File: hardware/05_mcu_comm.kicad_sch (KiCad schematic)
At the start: 0 parts

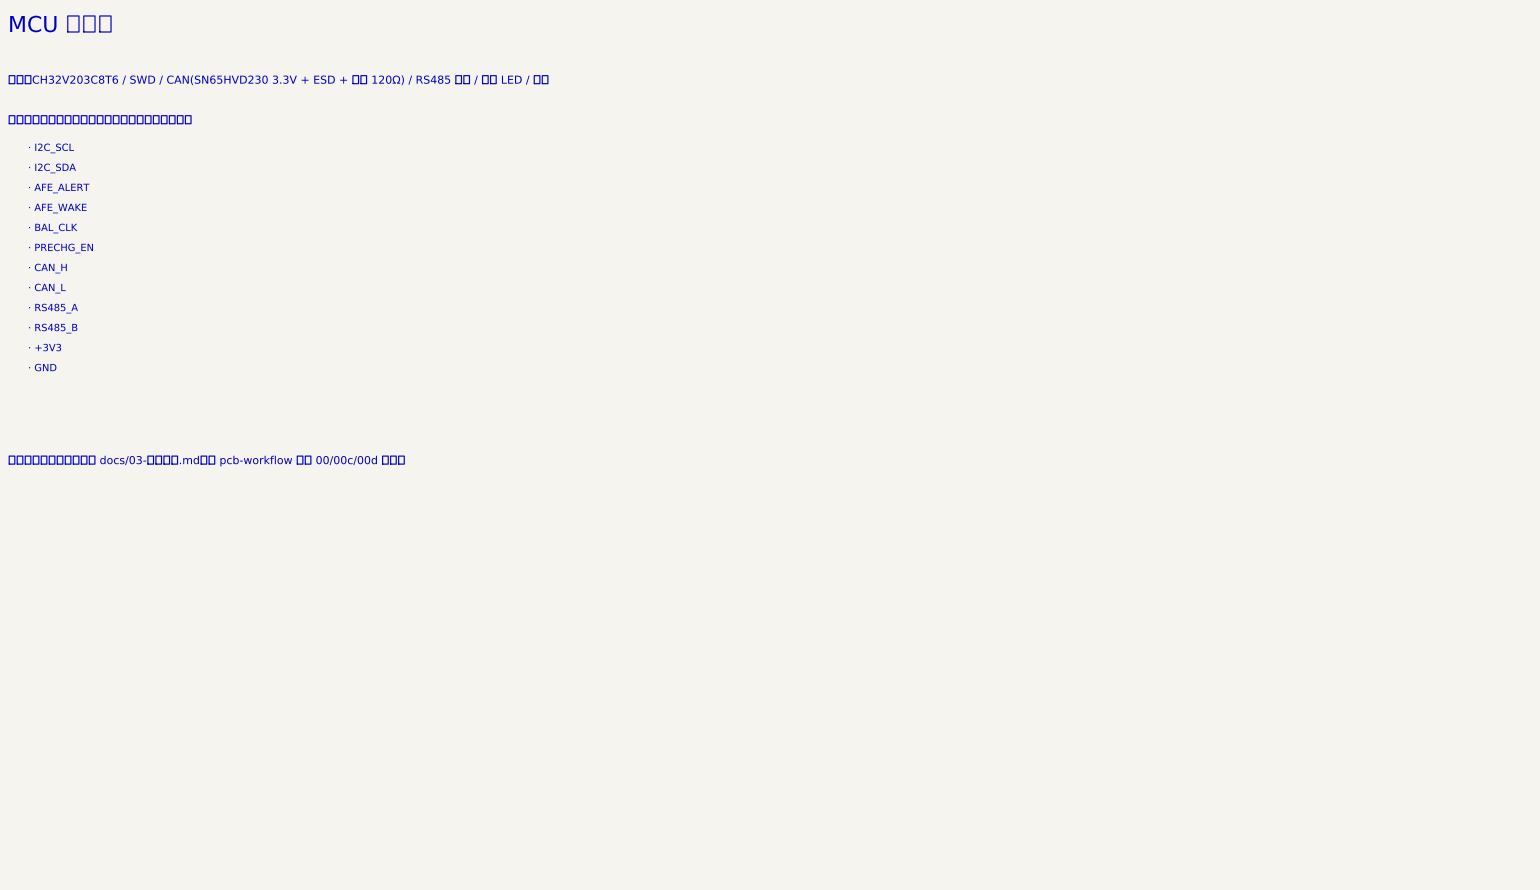
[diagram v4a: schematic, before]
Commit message: 05 页第 1 轮（DeepSeek，结尾因 API 余额不足 402 中断）：32 器件，ERC 仅跨页 isolated_pin_label，几何自检通过；取库 JP1 C492401
Co-Authored-By: Claude Opus 5.5 <noreply@anthropic.com>
Claude-Session: https://claude.ai/code/session_018LcBBXJnjJ1MVmds7Fkezv
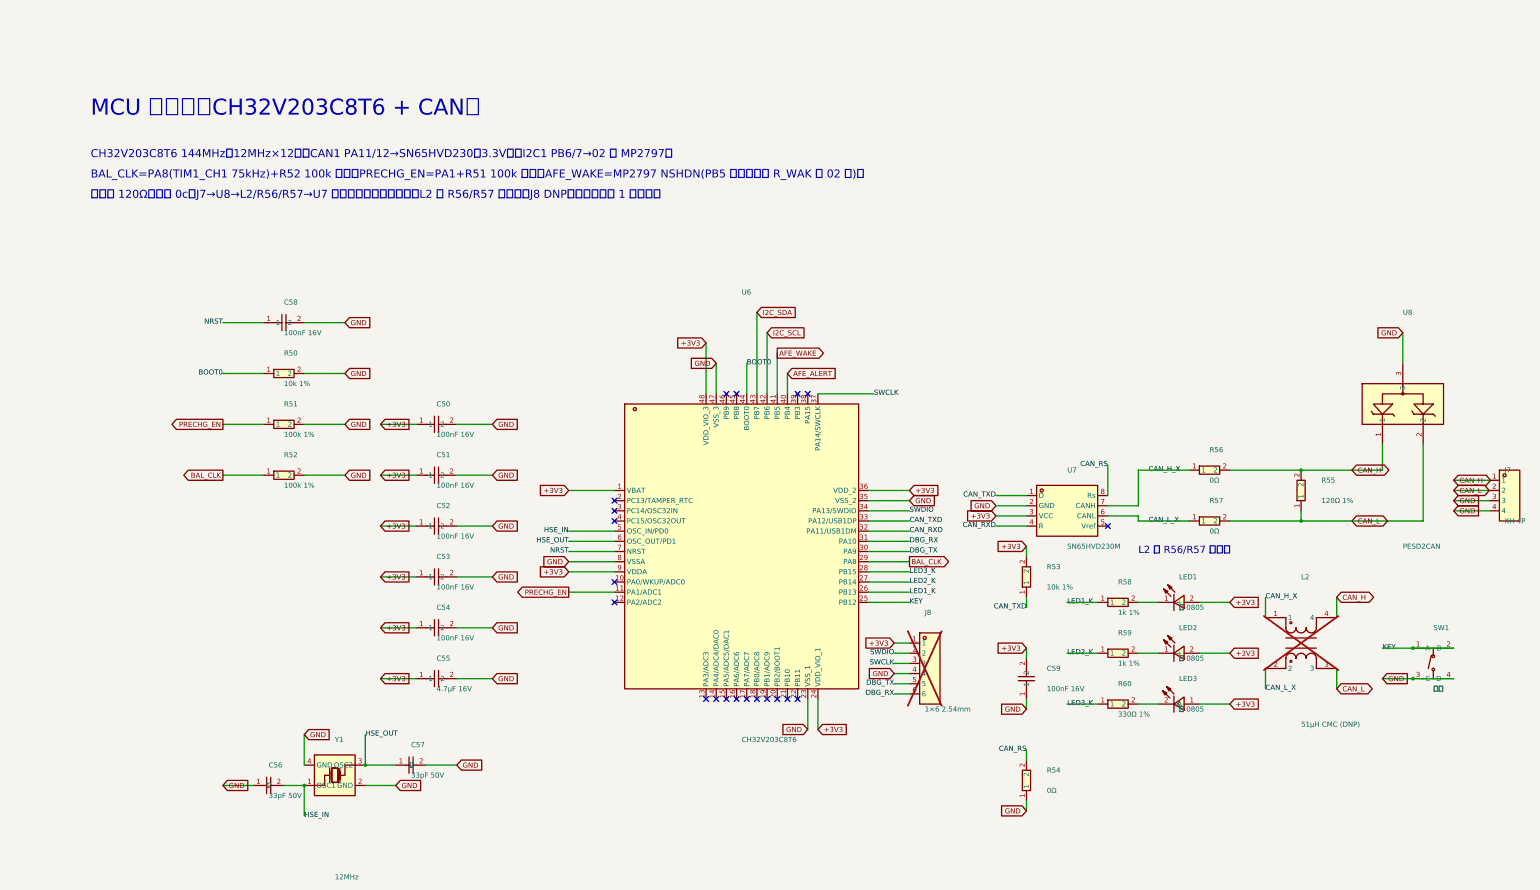
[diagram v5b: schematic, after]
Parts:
- added C50, C51, C52, C53, C54, C58, C59: 100nF 16V, jlc:C0402, symbol jlc:CL05B104KO5NNNC
- added C55: 4.7µF 16V, jlc:C0603, symbol jlc:CL10A475KO8NNNC
- added C56, C57: 33pF 50V, jlc:C0402, symbol jlc:0402CG330J500NT
- added J7: XH 4P, jlc:CONN-TH_4P-P2.50_4PIN, symbol jlc:ZX-XH2.54-4PZZ
- added J8: 1×6 2.54mm, jlc:HDR-TH_6P-P2.54-V-M, symbol jlc:PZ254V-11-06P
- added L2: 51µH CMC (DNP), jlc:FILTER-SMD_4P-L3.2-W2.5-BL_ACT1210, symbol jlc:ACT1210-510-2P-TL00
- added LED1, LED2: 红 0805, jlc:LED0805-RD, symbol jlc:FC-2012HRK-620D
- added LED3: 绿 0805, jlc:LED0805-R-RD, symbol jlc:0805G
- added R50, R53: 10k 1%, jlc:R0402, symbol jlc:0402WGF1002TCE
- added R51, R52: 100k 1%, jlc:R0402, symbol jlc:0402WGF1003TCE
- added R54, R56, R57: 0Ω, jlc:R0402, symbol jlc:0402WGF0000TCE
- added R55: 120Ω 1%, jlc:R0603, symbol jlc:0603WAF1200T5E
- added R58, R59: 1k 1%, jlc:R0402, symbol jlc:0402WGF1001TCE
- added R60: 330Ω 1%, jlc:R0402, symbol jlc:0402WGF3300TCE
- added SW1: 按键, jlc:SW-SMD_4P-L5.1-W5.1-P3.70-LS6.5-TL_H1.5, symbol jlc:TS-1187A-B-A-B
- added U6: CH32V203C8T6, jlc:LQFP-48_L7.0-W7.0-P0.50-LS9.0-BL, symbol jlc:CH32V203C8T6
- added U7: SN65HVD230M, jlc:SOIC-8_L5.0-W4.0-P1.27-LS6.0-BL, symbol jlc:SN65HVD230M_TR-HG
- added U8: PESD2CAN, jlc:SOT-23-3_L2.9-W1.3-P1.90-LS2.4-BR, symbol jlc:PESD2CAN_C2687131
- added Y1: 12MHz, jlc:CRYSTAL-SMD_4P-L3.2-W2.5-BL, symbol jlc:X322512MSB4SI
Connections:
- new net: LED2.1 (-), R59.2
- new net: LED1.1 (-), R58.2
- new net: LED3.2 (K), R60.2
- new net +3V3: C50.1, C51.1, C52.1, C53.1, C54.1, C55.1, C59.2, J8.1, LED1.2 (+), LED2.2 (+), LED3.1 (A), R53.2, U6.1 (VBAT), U6.24 (VDD_VIO_1), U6.36 (VDD_2), U6.48 (VDD_VIO_3), U6.9 (VDDA), U7.3 (VCC)
- new net AFE_ALERT: U6.40 (PB4)
- new net AFE_WAKE: U6.41 (PB5)
- new net BAL_CLK: R52.1, U6.29 (PA8)
- new net BOOT0: R50.1, U6.44 (BOOT0)
- new net CAN_H: J7.1, L2.4, R55.2, R56.2, U8.1
- new net CAN_H_X: L2.1, R56.1, U7.7 (CANH)
- new net CAN_L: J7.2, L2.3, R55.1, R57.2, U8.2
- new net CAN_L_X: L2.2, R57.1, U7.6 (CANL)
- new net CAN_RS: R54.2, U7.8 (Rs)
- new net CAN_RXD: U6.32 (PA11/USB1DM), U7.4 (R)
- new net CAN_TXD: R53.1, U6.33 (PA12/USB1DP), U7.1 (D)
- new net DBG_RX: J8.6, U6.31 (PA10)
- new net DBG_TX: J8.5, U6.30 (PA9)
- new net GND: C50.2, C51.2, C52.2, C53.2, C54.2, C55.2, C56.1, C57.2, C58.2, C59.1, J7.3, J7.4, J8.4, R50.2, R51.2, R52.2, R54.1, SW1.3 (C), SW1.4 (D), U6.23 (VSS_1), U6.35 (VSS_2), U6.47 (VSS_3), U6.8 (VSSA), U7.2 (GND), U8.3, Y1.2 (GND), Y1.4 (GND)
- new net HSE_IN: C56.2, U6.5 (OSC_IN/PD0), Y1.1 (OSC1)
- new net HSE_OUT: C57.1, U6.6 (OSC_OUT/PD1), Y1.3 (OSC2)
- new net I2C_SCL: U6.42 (PB6)
- new net I2C_SDA: U6.43 (PB7)
- new net KEY: SW1.1 (A), SW1.2 (B), U6.25 (PB12)
- new net LED1_K: R58.1, U6.26 (PB13)
- new net LED2_K: R59.1, U6.27 (PB14)
- new net LED3_K: R60.1, U6.28 (PB15)
- new net NRST: C58.1, U6.7 (NRST)
- new net PRECHG_EN: R51.1, U6.11 (PA1/ADC1)
- new net SWCLK: J8.3, U6.37 (PA14/SWCLK)
- new net SWDIO: J8.2, U6.34 (PA13/SWDIO)
- no-connect marks 0 -> 20
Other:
- note added: "BAL_CLK=PA8(TIM1_CH1 75kHz)+R52 100k 下拉；PRECHG_EN=PA1+R51 100k 下拉；AFE_WAKE=MP2797 NSHDN(PB5 开漏，上拉 R_WAK 在 02 页)；"
- note added: "CH32V203C8T6 144MHz（12MHz×12）；CAN1 PA11/12→SN65HVD230（3.3V）；I2C1 PB6/7→02 页 MP2797；"
- note added: "L2 与 R56/R57 二选一"
- note added: "MCU 与通讯（CH32V203C8T6 + CAN）"
- note added: "差分对 120Ω（规则 0c：J7→U8→L2/R56/R57→U7 直通道，顶层不换层）；L2 与 R56/R57 二选一；J8 DNP，下载器勿从 1 脚供电。"
- note removed: "MCU 与通讯"
- note removed: "· +3V3"
- note removed: "· AFE_ALERT"
- note removed: "· AFE_WAKE"
- note removed: "· BAL_CLK"
- note removed: "· CAN_H"
- note removed: "· CAN_L"
- note removed: "· GND"
- note removed: "· I2C_SCL"
- note removed: "· I2C_SDA"
- note removed: "· PRECHG_EN"
- note removed: "· RS485_A"
- note removed: "· RS485_B"
- note removed: "内容：CH32V203C8T6 / SWD / CAN(SN65HVD230 3.3V + ESD + 可选 120Ω) / RS485 可选 / 状态 LED / 按键"
- note removed: "接口网络（跨页用全局标签，名称以本清单为准）："
- note removed: "状态：待画。详细设计见 docs/03-详细设计.md；按 pcb-workflow 规则 00/00c/00d 执行。"

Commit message: 05 页第 2 轮中间产物（DeepSeek 跑满 1 小时超时）：JP1/CAN_TERM 已加；自检尚余 J7 字段压本体
Co-Authored-By: Claude Opus 5.5 <noreply@anthropic.com>
Claude-Session: https://claude.ai/code/session_018LcBBXJnjJ1MVmds7Fkezv
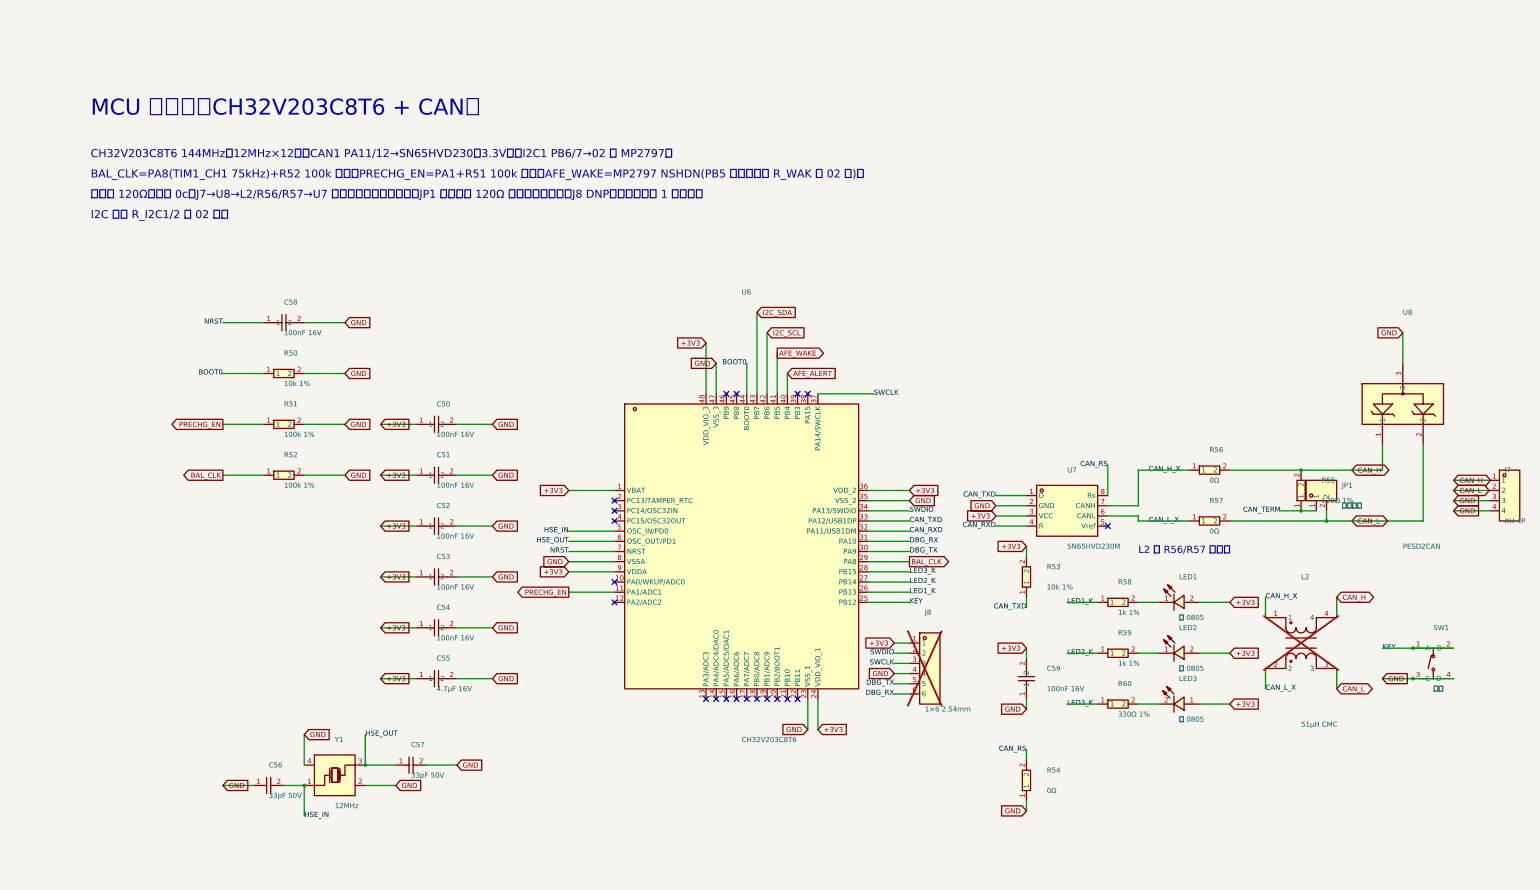
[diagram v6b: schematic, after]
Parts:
- added JP1: 终端跳线, jlc:HDR-TH_2P-P2.54-V-M, symbol jlc:PZ254V-11-02P
- L2: value 51µH CMC (DNP) -> 51µH CMC
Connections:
- net CAN_L: now also JP1.2; no longer R55.1
- new net CAN_TERM: JP1.1, R55.1
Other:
- note added: "I2C 上拉 R_I2C1/2 在 02 页。"
- note added: "差分对 120Ω（规则 0c：J7→U8→L2/R56/R57→U7 直通道，顶层不换层）；JP1 插帽接入 120Ω 终端，拔帽不用；J8 DNP，下载器勿从 1 脚供电。"
- note removed: "差分对 120Ω（规则 0c：J7→U8→L2/R56/R57→U7 直通道，顶层不换层）；L2 与 R56/R57 二选一；J8 DNP，下载器勿从 1 脚供电。"
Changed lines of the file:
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@@
 		)
 	)
-	(text "差分对 120Ω（规则 0c：J7→U8→L2/R56/R57→U7 直通道，顶层不换层）；L2 与 R56/R57 二选一；J8 DNP，下载器勿从 1 脚供电。"
+	(text "差分对 120Ω（规则 0c：J7→U8→L2/R56/R57→U7 直通道，顶层不换层）；JP1 插帽接入 120Ω 终端，拔帽不用；J8 DNP，下载器勿从 1 脚供电。"
 		(exclude_from_sim no)
 		(at 40.64 63.50 0)
@@
 		)
 	)
+	(text "I2C 上拉 R_I2C1/2 在 02 页。"
+		(exclude_from_sim no)
+		(at 40.64 68.58 0)
+		(effects
+			(font
+				(size 2.00 2.00)
+			)
+			(justify left top)
+		)
+	)
 	(wire
 		(pts
@@
 				(size 1.27 1.27)
 			)
-			(justify left)
+			(justify right)
 		)
 	)
@@
 	(wire
 		(pts
-			(xy 342.90 143.51)
-			(xy 342.90 146.05)
+			(xy 363.22 133.35)
+			(xy 342.90 133.35)
 		)
 		(stroke
@@
 	(wire
 		(pts
-			(xy 363.22 133.35)
 			(xy 342.90 133.35)
+			(xy 325.12 133.35)
 		)
 		(stroke
@@
 	(wire
 		(pts
-			(xy 342.90 133.35)
-			(xy 325.12 133.35)
+			(xy 342.90 143.51)
+			(xy 346.71 143.51)
+		)
+		(stroke
+			(width 0)
+			(type default)
+		)
+	)
+	(wire
+		(pts
+			(xy 342.90 143.51)
+			(xy 337.82 143.51)
+		)
+		(stroke
+			(width 0)
+			(type default)
+		)
+	)
+	(label "CAN_TERM"
+		(at 337.82 143.51 0)
+		(effects
+			(font
+				(size 1.27 1.27)
+			)
+			(justify right)
+		)
+	)
+	(wire
+		(pts
+			(xy 349.25 143.51)
+			(xy 349.25 146.05)
 		)
 		(stroke
@@
 		(pts
 			(xy 373.38 146.05)
-			(xy 342.90 146.05)
+			(xy 349.25 146.05)
 		)
 		(stroke
@@
 	(wire
 		(pts
-			(xy 342.90 146.05)
+			(xy 349.25 146.05)
 			(xy 325.12 146.05)
 		)
@@
 	)
 	(junction (at 342.90 133.35) (diameter 0) (color 0 0 0 0))
-	(junction (at 342.90 146.05) (diameter 0) (color 0 0 0 0))
+	(junction (at 342.90 143.51) (diameter 0) (color 0 0 0 0))
+	(junction (at 349.25 146.05) (diameter 0) (color 0 0 0 0))
 	(wire
 		(pts
@@
 		)
 		(property "Value" "12MHz"
-			(at 101.60 234.95 0)
+			(at 101.60 217.17 0)
 			(effects
 				(font
@@
 	)
 	(symbol
+		(lib_id "jlc:PZ254V-11-02P")
+		(at 347.98 139.70 90)
+		(unit 1)
+		(exclude_from_sim no)
+		(in_bom yes)
+		(on_board yes)
+		(dnp no)
+		(property "Reference" "JP1"
+			(at 353.06 137.16 270)
+			(effects
+				(font
+					(size 1.27 1.27)
+				)
+				(justify left)
+			)
+		)
+		(property "Value" "终端跳线"
+			(at 353.06 142.24 270)
+			(effects
+				(font
+					(size 1.27 1.27)
+				)
+				(justify left)
+			)
+		)
+		(property "Footprint" "jlc:HDR-TH_2P-P2.54-V-M"
+			(at 347.98 147.32 0)
+			(effects
+				(font
+					(size 1.27 1.27)
+				)
+				(justify left)
+				hide
+			)
+		)
+		(property "Datasheet" "https://lcsc.com/product-detail/New-Arrivals_XFCN-PZ254V-11-02P_C492401.html"
+			(at 347.98 147.32 0)
+			(effects
+				(font
+					(size 1.27 1.27)
+				)
+				(justify left)
+				hide
+			)
+		)
+		(property "LCSC" "C492401"
+			(at 347.98 147.32 0)
+			(effects
+				(font
+					(size 1.27 1.27)
+				)
+				(justify left)
+				hide
+			)
+		)
+		(pin "1")
+		(pin "2")
+		(instances
+			(project "mp2645a-bms"
+				(path "/632f74a5-cd8f-58d8-9ac1-1bfbb611d555/0739f2da-d4a5-5124-931f-263baaef6ebe"
+					(reference "JP1")
+					(unit 1)
+				)
+			)
+		)
+	)
+	(symbol
 		(lib_id "jlc:0402WGF0000TCE")
 		(at 320.04 133.35 0)
@@
 			)
 		)
-		(property "Value" "51µH CMC (DNP)"
+		(property "Value" "51µH CMC"
 			(at 342.90 196.85 0)
 			(effects
@@
 		)
 		(property "Value" "红 0805"
-			(at 312.42 167.64 0)
+			(at 312.42 170.18 0)
 			(effects
 				(font
@@
 		)
 		(property "Value" "红 0805"
-			(at 312.42 180.34 0)
+			(at 312.42 182.88 0)
 			(effects
 				(font
@@
 		)
 		(property "Value" "绿 0805"
-			(at 312.42 193.04 0)
+			(at 312.42 195.58 0)
 			(effects
 				(font
